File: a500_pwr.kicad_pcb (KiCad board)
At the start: 2 copper layers, 28.8 x 43.8 mm, 20 parts, among them J1 PJ-102A, J2 APWR_big, J3 APWR_small, SW1 RMS1R102M7QES, U1 LMZM23600SILR, U2 RPM5.0-6.0

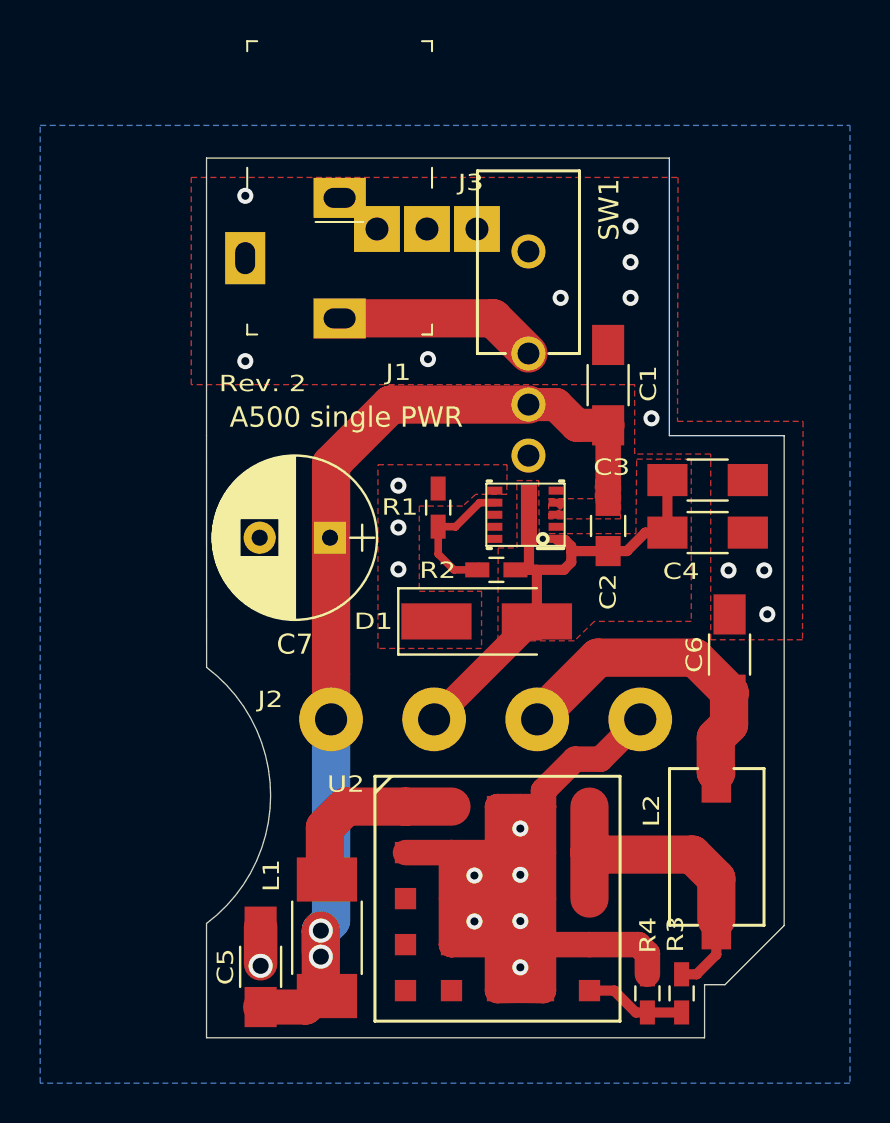
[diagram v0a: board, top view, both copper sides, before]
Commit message: adjust for different Barrel connector and note about R3/R4
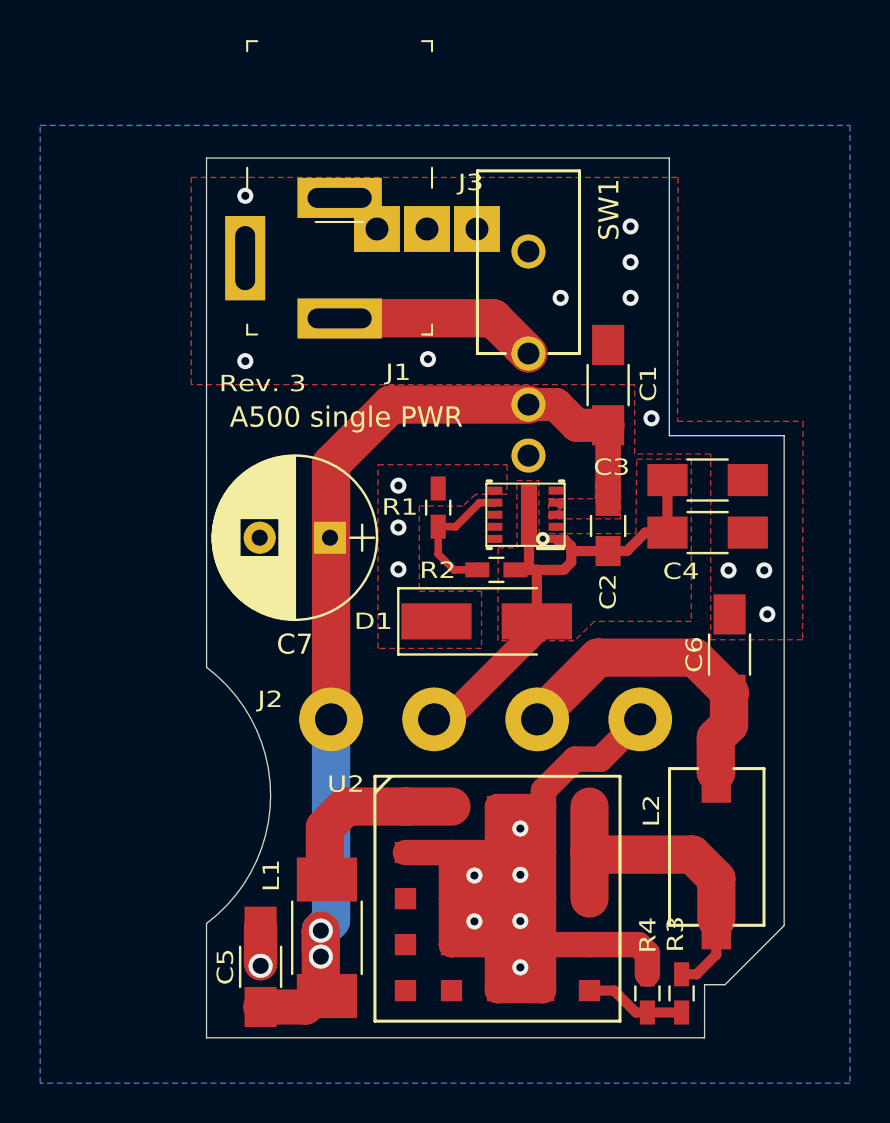
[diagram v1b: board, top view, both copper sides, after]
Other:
- board text added: "Rev. 3"
- board text removed: "Rev. 2"
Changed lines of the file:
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@@
     (thickness 1.6)
     (drawings 17)
-    (tracks 134)
+    (tracks 136)
     (zones 0)
     (modules 20)
@@
     (add_net "Net-(U2-PadE1)")
     (add_net "Net-(U2-PadE2)")
+  )
+  (module a500_pwr:Barrel_Jack_5.5mmODx2.1mmID_PJ-102A (layer F.Cu)
+    (at 62.2 113.5926)
+    (fp_text reference J1 (at 2.9224 5.6858) (layer F.SilkS)
+      (effects (font (size 0.8128 1) (thickness 0.2032)))
+    )
+    (fp_text value PJ-102A (at 0 5.8) (layer F.Fab)
+      (effects (font (size 1 1) (thickness 0.15)))
+    )
+    (fp_line (start -5.9 4.25) (end 4.8 4.25) (layer F.CrtYd) (width 0.05))
+    (fp_line (start 4.8 -10.95) (end 4.8 4.25) (layer F.CrtYd) (width 0.05))
+    (fp_line (start -5.9 -10.95) (end -5.9 4.25) (layer F.CrtYd) (width 0.05))
+    (fp_line (start -5.9 -10.95) (end 4.8 -10.95) (layer F.CrtYd) (width 0.05))
+    (fp_line (start 4.6 -3.5) (end 4.6 -4.5) (layer F.SilkS) (width 0.1))
+    (fp_line (start -4.6 -3.5) (end -4.6 -4.5) (layer F.SilkS) (width 0.1))
+    (fp_line (start 4.6 -10.8) (end 4.6 -10.3) (layer F.SilkS) (width 0.1))
+    (fp_line (start 4.6 -10.8) (end 4.1 -10.8) (layer F.SilkS) (width 0.1))
+    (fp_line (start -4.6 -10.8) (end -4.1 -10.8) (layer F.SilkS) (width 0.1))
+    (fp_line (start -4.6 -10.8) (end -4.6 -10.3) (layer F.SilkS) (width 0.1))
+    (fp_line (start -1.2 -1.8) (end 1.2 -1.8) (layer F.SilkS) (width 0.1))
+    (fp_line (start -4.6 3.8) (end -4.6 3.3) (layer F.SilkS) (width 0.1))
+    (fp_line (start -4.6 3.8) (end -4.1 3.8) (layer F.SilkS) (width 0.1))
+    (fp_line (start 4.6 3.8) (end 4.6 3.3) (layer F.SilkS) (width 0.1))
+    (fp_line (start 4.6 3.8) (end 4.1 3.8) (layer F.SilkS) (width 0.1))
+    (fp_line (start -4.5 -10.7) (end 4.5 -10.7) (layer F.Fab) (width 0.1))
+    (fp_line (start 4.5 3.7) (end 4.5 -10.7) (layer F.Fab) (width 0.1))
+    (fp_line (start -4.5 3.7) (end -4.5 -10.7) (layer F.Fab) (width 0.1))
+    (fp_line (start -4.5 3.7) (end 4.5 3.7) (layer F.Fab) (width 0.1))
+    (pad 3 thru_hole rect (at -4.7 0) (size 2 4.2) (drill oval 1 3.2) (layers *.Cu *.Mask)
+      (net 1 GND))
+    (pad 1 thru_hole rect (at 0 3) (size 4.2 2) (drill oval 3.2 1) (layers *.Cu *.Mask)
+      (net 17 /SW12V))
+    (pad 2 thru_hole rect (at 0 -3) (size 4.2 2) (drill oval 3.2 1) (layers *.Cu *.Mask)
+      (net 1 GND))
+    (model ${KIPRJMOD}/3d/CUI_DEVICES_PJ-102A.step
+      (offset (xyz 0 10.7 6.5))
+      (scale (xyz 1 1 1))
+      (rotate (xyz -90 0 -90))
+    )
   )
   (module a500_pwr:rock_sw (layer F.Cu)
@@
       (net 2 +12V))
   )
-  (module a500_pwr:Barrel_Jack_5.5mmODx2.1mmID_PJ-102A (layer F.Cu)
-    (at 62.2 113.5926)
-    (fp_text reference J1 (at 2.9224 5.6858) (layer F.SilkS)
-      (effects (font (size 0.8128 1) (thickness 0.2032)))
-    )
-    (fp_text value PJ-102A (at 0 5.8) (layer F.Fab)
-      (effects (font (size 1 1) (thickness 0.15)))
-    )
-    (fp_line (start -5.9 4.25) (end 4.8 4.25) (layer F.CrtYd) (width 0.05))
-    (fp_line (start 4.8 -10.95) (end 4.8 4.25) (layer F.CrtYd) (width 0.05))
-    (fp_line (start -5.9 -10.95) (end -5.9 4.25) (layer F.CrtYd) (width 0.05))
-    (fp_line (start -5.9 -10.95) (end 4.8 -10.95) (layer F.CrtYd) (width 0.05))
-    (fp_line (start 4.6 -3.5) (end 4.6 -4.5) (layer F.SilkS) (width 0.1))
-    (fp_line (start -4.6 -3.5) (end -4.6 -4.5) (layer F.SilkS) (width 0.1))
-    (fp_line (start 4.6 -10.8) (end 4.6 -10.3) (layer F.SilkS) (width 0.1))
-    (fp_line (start 4.6 -10.8) (end 4.1 -10.8) (layer F.SilkS) (width 0.1))
-    (fp_line (start -4.6 -10.8) (end -4.1 -10.8) (layer F.SilkS) (width 0.1))
-    (fp_line (start -4.6 -10.8) (end -4.6 -10.3) (layer F.SilkS) (width 0.1))
-    (fp_line (start -1.2 -1.8) (end 1.2 -1.8) (layer F.SilkS) (width 0.1))
-    (fp_line (start -4.6 3.8) (end -4.6 3.3) (layer F.SilkS) (width 0.1))
-    (fp_line (start -4.6 3.8) (end -4.1 3.8) (layer F.SilkS) (width 0.1))
-    (fp_line (start 4.6 3.8) (end 4.6 3.3) (layer F.SilkS) (width 0.1))
-    (fp_line (start 4.6 3.8) (end 4.1 3.8) (layer F.SilkS) (width 0.1))
-    (fp_line (start -4.5 -10.7) (end 4.5 -10.7) (layer F.Fab) (width 0.1))
-    (fp_line (start 4.5 3.7) (end 4.5 -10.7) (layer F.Fab) (width 0.1))
-    (fp_line (start -4.5 3.7) (end -4.5 -10.7) (layer F.Fab) (width 0.1))
-    (fp_line (start -4.5 3.7) (end 4.5 3.7) (layer F.Fab) (width 0.1))
-    (pad 3 thru_hole rect (at -4.7 0) (size 2 2.6) (drill oval 1 1.6) (layers *.Cu *.Mask)
-      (net 1 GND))
-    (pad 1 thru_hole rect (at 0 3) (size 2.6 2) (drill oval 1.6 1) (layers *.Cu *.Mask)
-      (net 17 /SW12V))
-    (pad 2 thru_hole rect (at 0 -3) (size 2.6 2) (drill oval 1.6 1) (layers *.Cu *.Mask)
-      (net 1 GND))
-    (model ${KIPRJMOD}/3d/CUI_DEVICES_PJ-102A.step
-      (offset (xyz 0 10.7 6.5))
-      (scale (xyz 1 1 1))
-      (rotate (xyz -90 0 -90))
-    )
-  )
   (module Diodes_SMD:D_SMA_Handsoldering (layer F.Cu)
     (at 69.5198 131.6736)
@@
     (arrow2b (pts (xy 51.3334 108.6104) (xy 51.919821 109.736904)))
   )
-  (gr_text "Rev. 2" (at 58.3692 119.8372) (layer F.SilkS)
+  (gr_text "Rev. 3" (at 58.3692 119.8372) (layer F.SilkS)
     (effects (font (size 0.8128 1) (thickness 0.2032)))
   )
@@
   (segment (start 73.3552 129.1082) (end 73.406 129.0574) (width 0.508) (layer F.Cu) (net 3))
   (segment (start 70.9524 129.1082) (end 73.3552 129.1082) (width 0.508) (layer F.Cu) (net 3))
-  (segment (start 72.0198 131.4346) (end 66.904 136.5504) (width 1.27) (layer F.Cu) (net 3))
   (segment (start 72.0198 131.6736) (end 72.0198 131.9934) (width 1.27) (layer F.Cu) (net 3))
   (segment (start 73.7308 128.1738) (end 75.565 128.1738) (width 0.508) (layer F.Cu) (net 3))
@@
   (segment (start 75.565 128.1738) (end 76.4994 128.1738) (width 0.508) (layer F.Cu) (net 3))
   (segment (start 76.4994 128.1738) (end 77.4192 127.254) (width 0.508) (layer F.Cu) (net 3))
+  (segment (start 67.5767 136.5504) (end 66.904 136.5504) (width 1.27) (layer F.Cu) (net 3))
+  (segment (start 72.0198 131.4346) (end 72.0198 132.1073) (width 1.27) (layer F.Cu) (net 3))
+  (segment (start 72.0198 132.1073) (end 67.5767 136.5504) (width 1.27) (layer F.Cu) (net 3))
   (segment (start 80.9244 137.4648) (end 81.5848 136.8044) (width 1.905) (layer F.Cu) (net 4))
   (segment (start 81.5848 136.8044) (end 81.5848 135.35) (width 1.905) (layer F.Cu) (net 4))
